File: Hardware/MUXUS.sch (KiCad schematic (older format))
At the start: 124 parts, among them J1 USB_C_Receptacle_USB2.0, J10 VCP, J2 USB_B, J3 USB_A, J4 USB_B, J5 USB_A, J6 STDC14, J7 USB_B, J8 USB_A, J9 SWD, SW1 USER, SW2 RESET, U1 USBLC6-4SC6, U10 AP2151W, U11 AOZ1212AI, U12 USBLC6-2SC6, U13 USBLC6-2SC6, U14 AP2151W, U2 USB2504A-JT, U3 USBLC6-2SC6, U4 USBLC6-2SC6, U5 AP2151W, U6 TS3USBCA420RSVR, U7 STM32G431K8T6, U8 USBLC6-2SC6, U9 USBLC6-2SC6, Y1 ATS240C

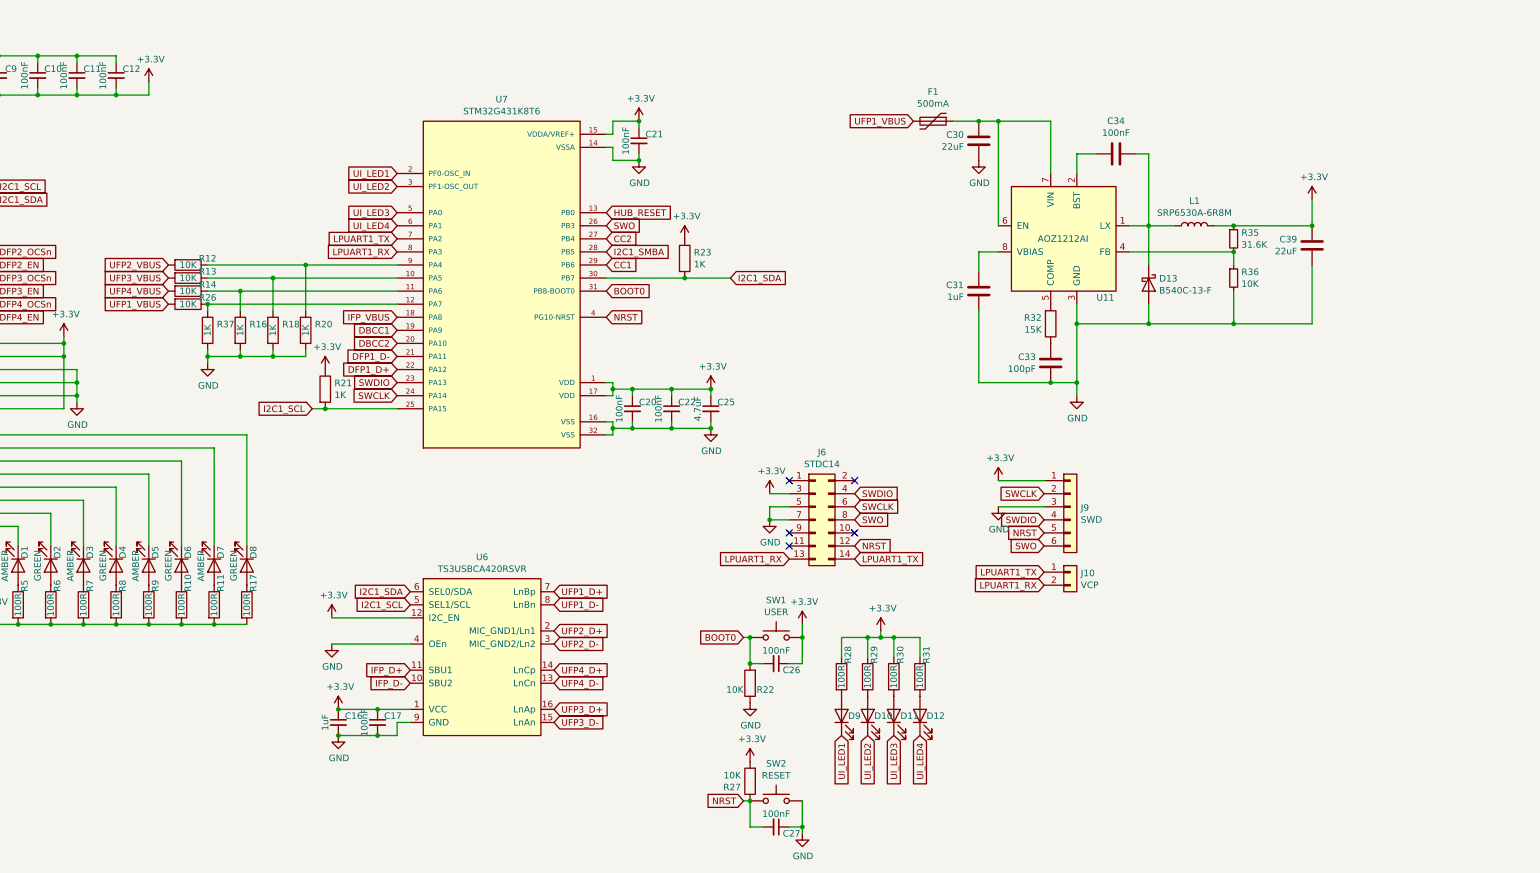
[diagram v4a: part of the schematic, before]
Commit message: Updated STM32G441KBU6
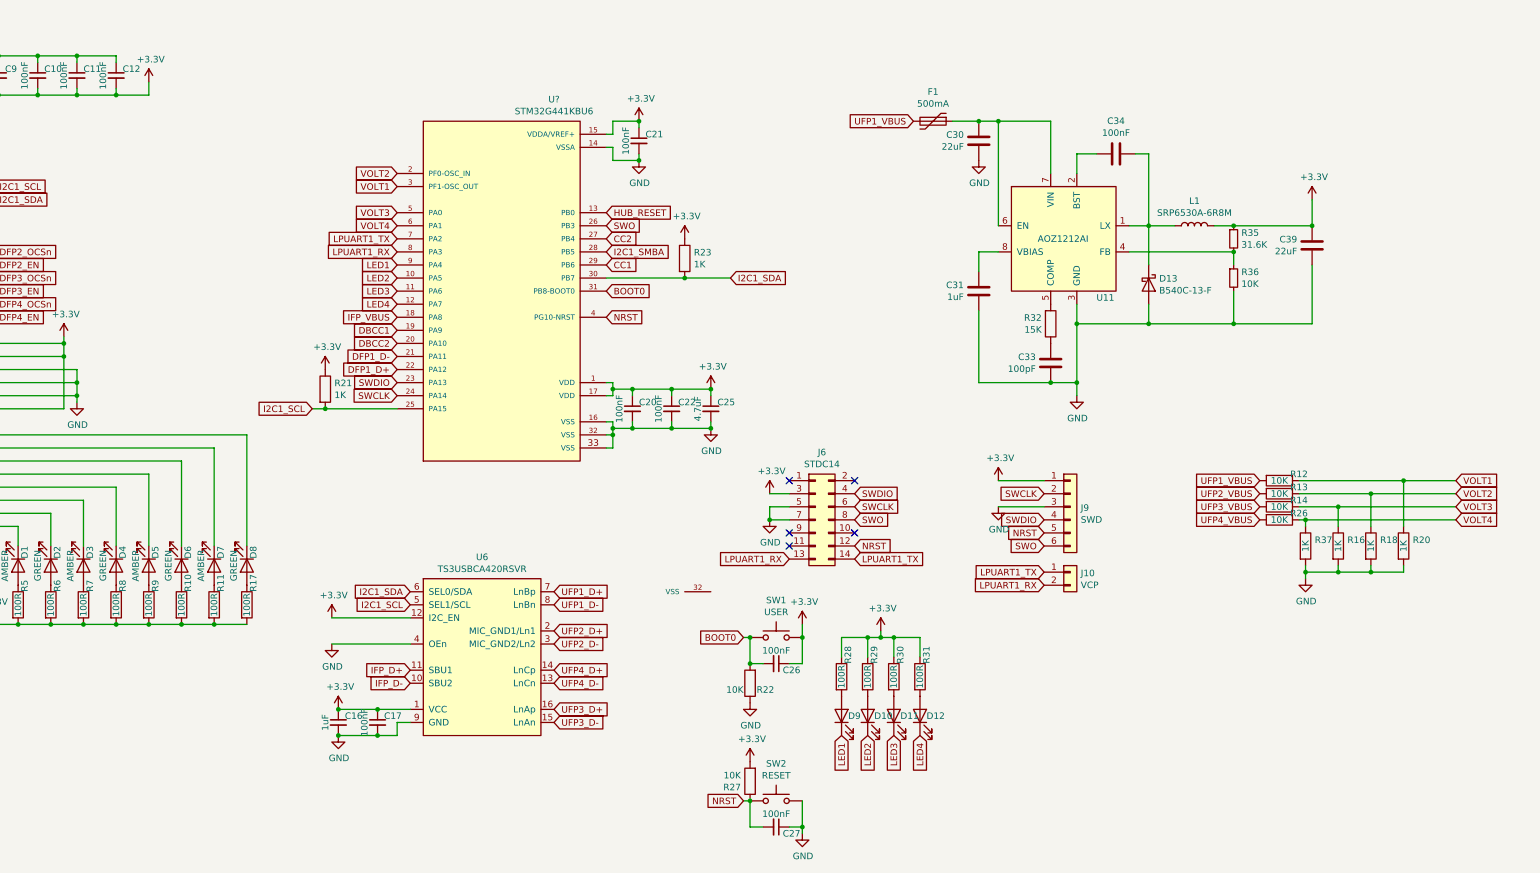
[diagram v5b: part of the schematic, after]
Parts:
- removed U7: STM32G431K8T6, STM32G431K8T6:STM32G431K8T6, symbol STM32G431K8T6:STM32G431K8T6
- added U?: STM32G441KBU6, STM32G441KBU6:STM32G441KBU6, symbol STM32G441KBU6:STM32G441KBU6
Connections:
- net +3V3: now also U?.1 (VDD), U?.15 (VDDA/VREF+), U?.17 (VDD)
- net BOOT0: now also U?.31 (PB8-BOOT0)
- net CC1: now also U?.19 (PA9), U?.29 (PB6)
- net CC2: now also U?.20 (PA10), U?.27 (PB4)
- net DFP1_D+: now also U?.22 (PA12)
- net DFP1_D-: now also U?.21 (PA11)
- net GND: now also U?.14 (VSSA), U?.16 (VSS), U?.32 (VSS), U?.33 (VSS)
- net HUB_RESET: now also U?.13 (PB0)
- net I2C1_SCL: now also U?.25 (PA15)
- net I2C1_SDA: now also U?.30 (PB7)
- net I2C1_SMBA: now also U?.28 (PB5)
- net IFP_VBUS: now also U?.18 (PA8)
- net LPUART1_RX: now also U?.8 (PA3)
- net LPUART1_TX: now also U?.7 (PA2)
- net NRST: now also U?.4 (PG10-NRST)
- net SWCLK: now also U?.24 (PA14)
- net SWDIO: now also U?.23 (PA13)
- net SWO: now also U?.26 (PB3)
- net UFP2_VBUS: now also R13.2; no longer R12.2
- net UFP3_VBUS: now also R14.2; no longer R13.2
- net UFP4_VBUS: now also R26.2; no longer R14.2
- net VBUS: now also R12.2; no longer R26.2
- net VOLT2: now reaches R13.1, R18.1
- net VOLT2: now also U?.2 (PF0-OSC_IN)
- net VOLT3: now reaches R14.1, R16.1
- net VOLT3: now also U?.5 (PA0)
- net VOLT4: now reaches R26.1, R37.1
- net VOLT4: now also U?.6 (PA1)
- net VOLT1: now reaches R12.1, R20.1
- net VOLT1: now also U?.3 (PF1-OSC_OUT)
- net UI_LED1 renamed LED1
- net LED1: now also U?.9 (PA4)
- net UI_LED2 renamed LED2
- net LED2: now also U?.10 (PA5)
- net UI_LED3 renamed LED3
- net LED3: now also U?.11 (PA6)
- net UI_LED4 renamed LED4
- net LED4: now also U?.12 (PA7)
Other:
- moved on the sheet: R12, R13, R14, R16, R18, R20, R26, R37
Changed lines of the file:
@@
 $EndDescr
 $Comp
-L STM32G431K8T6:STM32G431K8T6 U7
-U 1 1 61457F4C
-P 8100 6800
-F 0 "U7" H 8100 8267 50  0000 C CNN
-F 1 "STM32G431K8T6" H 8100 8176 50  0000 C CNN
-F 2 "STM32G431K8T6:STM32G431K8T6" H 8100 6800 50  0001 L BNN
-F 3 "https://www.st.com/en/microcontrollers-microprocessors/stm32g431k8.html#documentation" H 8100 6800 50  0001 L BNN
-F 4 "ST" H 8100 6800 50  0001 L BNN "MANUFACTURER"
-F 5 "2" H 8100 6800 50  0001 L BNN "PARTREV"
-F 6 "1.6mm" H 8100 6800 50  0001 L BNN "MAXIMUN_PACKAGE_HEIGHT"
-F 7 "IPC-7351B" H 8100 6800 50  0001 L BNN "STANDARD"
-	1    8100 6800
-	1    0    0    -1
-$EndComp
-$Comp
 L Device:C_Small C20
 U 1 1 614734E1
@@
 Text GLabel 8900 6200 2    50   Input ~ 0
 HUB_RESET
-Text GLabel 7300 6300 0    50   Input ~ 0
-UI_LED4
-Text GLabel 7300 6200 0    50   Input ~ 0
-UI_LED3
-Text GLabel 7300 6000 0    50   Input ~ 0
-UI_LED2
-Text GLabel 7300 5900 0    50   Input ~ 0
-UI_LED1
+Text GLabel 7300 6900 0    50   Input ~ 0
+LED4
+Text GLabel 7300 6800 0    50   Input ~ 0
+LED3
+Text GLabel 7300 6700 0    50   Input ~ 0
+LED2
+Text GLabel 7300 6600 0    50   Input ~ 0
+LED1
 Text GLabel 4200 6100 2    50   Input ~ 0
 I2C1_SDA
@@
 	4850 7650 4850 7600
 Text GLabel 11300 10200 3    50   Input ~ 0
-UI_LED4
+LED4
 $Comp
 L Device:LED D12
@@
 $EndComp
 Text GLabel 11100 10200 3    50   Input ~ 0
-UI_LED3
+LED3
 $Comp
 L Device:LED D11
@@
 $EndComp
 Text GLabel 10900 10200 3    50   Input ~ 0
-UI_LED2
+LED2
 $Comp
 L Device:LED D10
@@
 $EndComp
 Text GLabel 10700 10200 3    50   Input ~ 0
-UI_LED1
+LED1
 $Comp
 L Device:LED D9
@@
 L Device:R R14
 U 1 1 6241BDE6
-P 5700 6800
-F 0 "R14" V 5650 6950 50  0000 C CNN
-F 1 "10K" V 5700 6800 50  0000 C CNN
-F 2 "Resistor_SMD:R_1206_3216Metric" V 5630 6800 50  0001 C CNN
-F 3 "~" H 5700 6800 50  0001 C CNN
-	1    5700 6800
+P 14050 8450
+F 0 "R14" V 14000 8600 50  0000 C CNN
+F 1 "10K" V 14050 8450 50  0000 C CNN
+F 2 "Resistor_SMD:R_1206_3216Metric" V 13980 8450 50  0001 C CNN
+F 3 "~" H 14050 8450 50  0001 C CNN
+	1    14050 8450
 	0    1    1    0
 $EndComp
@@
 L Device:R R13
 U 1 1 6241B806
-P 5700 6700
-F 0 "R13" V 5650 6850 50  0000 C CNN
-F 1 "10K" V 5700 6700 50  0000 C CNN
-F 2 "Resistor_SMD:R_1206_3216Metric" V 5630 6700 50  0001 C CNN
-F 3 "~" H 5700 6700 50  0001 C CNN
-	1    5700 6700
+P 14050 8350
+F 0 "R13" V 14000 8500 50  0000 C CNN
+F 1 "10K" V 14050 8350 50  0000 C CNN
+F 2 "Resistor_SMD:R_1206_3216Metric" V 13980 8350 50  0001 C CNN
+F 3 "~" H 14050 8350 50  0001 C CNN
+	1    14050 8350
 	0    1    1    0
 $EndComp
@@
 L Device:R R12
 U 1 1 62418C95
-P 5700 6600
-F 0 "R12" V 5650 6750 50  0000 C CNN
-F 1 "10K" V 5700 6600 50  0000 C CNN
-F 2 "Resistor_SMD:R_1206_3216Metric" V 5630 6600 50  0001 C CNN
-F 3 "~" H 5700 6600 50  0001 C CNN
-	1    5700 6600
+P 14050 8250
+F 0 "R12" V 14000 8400 50  0000 C CNN
+F 1 "10K" V 14050 8250 50  0000 C CNN
+F 2 "Resistor_SMD:R_1206_3216Metric" V 13980 8250 50  0001 C CNN
+F 3 "~" H 14050 8250 50  0001 C CNN
+	1    14050 8250
 	0    1    1    0
 $EndComp
-Text GLabel 5550 6800 0    50   Input ~ 0
+Text GLabel 13900 8550 0    50   Input ~ 0
 UFP4_VBUS
-Text GLabel 5550 6700 0    50   Input ~ 0
+Text GLabel 13900 8450 0    50   Input ~ 0
 UFP3_VBUS
-Text GLabel 5550 6600 0    50   Input ~ 0
+Text GLabel 13900 8350 0    50   Input ~ 0
 UFP2_VBUS
 $Comp
 L Device:R R20
 U 1 1 62488B54
-P 6600 7100
-F 0 "R20" H 6670 7146 50  0000 L CNN
-F 1 "1K" V 6600 7100 50  0000 C CNN
-F 2 "Resistor_SMD:R_1206_3216Metric" V 6530 7100 50  0001 C CNN
-F 3 "~" H 6600 7100 50  0001 C CNN
-	1    6600 7100
+P 15000 8750
+F 0 "R20" H 15070 8796 50  0000 L CNN
+F 1 "1K" V 15000 8750 50  0000 C CNN
+F 2 "Resistor_SMD:R_1206_3216Metric" V 14930 8750 50  0001 C CNN
+F 3 "~" H 15000 8750 50  0001 C CNN
+	1    15000 8750
 	1    0    0    -1
 $EndComp
@@
 L Device:R R18
 U 1 1 624DD996
-P 6350 7100
-F 0 "R18" H 6420 7146 50  0000 L CNN
-F 1 "1K" V 6350 7100 50  0000 C CNN
-F 2 "Resistor_SMD:R_1206_3216Metric" V 6280 7100 50  0001 C CNN
-F 3 "~" H 6350 7100 50  0001 C CNN
-	1    6350 7100
+P 14750 8750
+F 0 "R18" H 14820 8796 50  0000 L CNN
+F 1 "1K" V 14750 8750 50  0000 C CNN
+F 2 "Resistor_SMD:R_1206_3216Metric" V 14680 8750 50  0001 C CNN
+F 3 "~" H 14750 8750 50  0001 C CNN
+	1    14750 8750
 	1    0    0    -1
 $EndComp
 $Comp
-L Device:R R16
-U 1 1 624DE01E
-P 6100 7100
-F 0 "R16" H 6170 7146 50  0000 L CNN
-F 1 "1K" V 6100 7100 50  0000 C CNN
-F 2 "Resistor_SMD:R_1206_3216Metric" V 6030 7100 50  0001 C CNN
-F 3 "~" H 6100 7100 50  0001 C CNN
-	1    6100 7100
-	1    0    0    -1
-$EndComp
-Wire Wire Line
-	5850 6800 6100 6800
-$Comp
 L power:GND #PWR015
 U 1 1 6260B042
-P 5850 7350
-F 0 "#PWR015" H 5850 7100 50  0001 C CNN
-F 1 "GND" H 5855 7177 50  0000 C CNN
-F 2 "" H 5850 7350 50  0001 C CNN
-F 3 "" H 5850 7350 50  0001 C CNN
-	1    5850 7350
+P 14250 9000
+F 0 "#PWR015" H 14250 8750 50  0001 C CNN
+F 1 "GND" H 14255 8827 50  0000 C CNN
+F 2 "" H 14250 9000 50  0001 C CNN
+F 3 "" H 14250 9000 50  0001 C CNN
+	1    14250 9000
 	1    0    0    -1
 $EndComp
 Wire Wire Line
-	6350 7300 6100 7300
+	14750 8950 14500 8950
 Wire Wire Line
-	6100 7300 6100 7250
+	14500 8950 14500 8900
 Wire Wire Line
-	6350 7300 6350 7250
-Connection ~ 6350 7300
+	14750 8950 14750 8900
+Connection ~ 14750 8950
 Wire Wire Line
-	6350 7300 6600 7300
+	14750 8950 15000 8950
 Wire Wire Line
-	6600 7300 6600 7250
+	15000 8950 15000 8900
 $Comp
 L power:VBUS #PWR06
@@
 Text GLabel 12250 9050 0    50   Input ~ 0
 LPUART1_RX
-Wire Wire Line
-	5850 6600 6600 6600
-Wire Wire Line
-	5850 6700 6350 6700
 $Comp
 L Device:R R26
 U 1 1 615C410A
-P 5700 6900
-F 0 "R26" V 5650 7050 50  0000 C CNN
-F 1 "10K" V 5700 6900 50  0000 C CNN
-F 2 "Resistor_SMD:R_1206_3216Metric" V 5630 6900 50  0001 C CNN
-F 3 "~" H 5700 6900 50  0001 C CNN
-	1    5700 6900
+P 14050 8550
+F 0 "R26" V 14000 8700 50  0000 C CNN
+F 1 "10K" V 14050 8550 50  0000 C CNN
+F 2 "Resistor_SMD:R_1206_3216Metric" V 13980 8550 50  0001 C CNN
+F 3 "~" H 14050 8550 50  0001 C CNN
+	1    14050 8550
 	0    1    1    0
 $EndComp
-Wire Wire Line
-	7300 6900 5850 6900
 $Comp
 L Device:R R37
 U 1 1 6167BF5A
-P 5850 7100
-F 0 "R37" H 5920 7146 50  0000 L CNN
-F 1 "1K" V 5850 7100 50  0000 C CNN
-F 2 "Resistor_SMD:R_1206_3216Metric" V 5780 7100 50  0001 C CNN
-F 3 "~" H 5850 7100 50  0001 C CNN
-	1    5850 7100
+P 14250 8750
+F 0 "R37" H 14320 8796 50  0000 L CNN
+F 1 "1K" V 14250 8750 50  0000 C CNN
+F 2 "Resistor_SMD:R_1206_3216Metric" V 14180 8750 50  0001 C CNN
+F 3 "~" H 14250 8750 50  0001 C CNN
+	1    14250 8750
 	1    0    0    -1
 $EndComp
-Connection ~ 6100 7300
+Connection ~ 14500 8950
 Wire Wire Line
-	5850 7300 5850 7250
+	14250 8950 14250 8900
 Wire Wire Line
-	5850 7300 6100 7300
+	14250 8950 14500 8950
 Wire Wire Line
-	5850 7350 5850 7300
-Connection ~ 5850 7300
+	14250 9000 14250 8950
+Connection ~ 14250 8950
 Wire Wire Line
-	5850 6950 5850 6900
-Connection ~ 5850 6900
+	14250 8600 14250 8550
 Wire Wire Line
-	6100 6950 6100 6800
-Connection ~ 6100 6800
+	14500 8600 14500 8450
 Wire Wire Line
-	6100 6800 7300 6800
+	14750 8600 14750 8350
 Wire Wire Line
-	6350 6950 6350 6700
-Connection ~ 6350 6700
+	15000 8600 15000 8250
+Text GLabel 13900 8250 0    50   Input ~ 0
+UFP1_VBUS
 Wire Wire Line
-	6350 6700 7300 6700
+	14200 8550 14250 8550
+Connection ~ 14250 8550
+Text GLabel 15400 8250 2    50   Input ~ 0
+VOLT1
+Text GLabel 15400 8350 2    50   Input ~ 0
+VOLT2
+Text GLabel 15400 8450 2    50   Input ~ 0
+VOLT3
+Text GLabel 15400 8550 2    50   Input ~ 0
+VOLT4
+Text GLabel 7300 6000 0    50   Input ~ 0
+VOLT1
+Text GLabel 7300 5900 0    50   Input ~ 0
+VOLT2
+Text GLabel 7300 6200 0    50   Input ~ 0
+VOLT3
+Text GLabel 7300 6300 0    50   Input ~ 0
+VOLT4
+Wire Wire Line
+	14250 8550 15400 8550
+$Comp
+L Device:R R16
+U 1 1 624DE01E
+P 14500 8750
+F 0 "R16" H 14570 8796 50  0000 L CNN
+F 1 "1K" V 14500 8750 50  0000 C CNN
+F 2 "Resistor_SMD:R_1206_3216Metric" V 14430 8750 50  0001 C CNN
+F 3 "~" H 14500 8750 50  0001 C CNN
+	1    14500 8750
+	1    0    0    -1
+$EndComp
+Connection ~ 14500 8450
 Wire Wire Line
-	6600 6950 6600 6600
-Connection ~ 6600 6600
+	14500 8450 15400 8450
 Wire Wire Line
-	6600 6600 7300 6600
-Text GLabel 5550 6900 0    50   Input ~ 0
-UFP1_VBUS
+	14200 8450 14500 8450
+Connection ~ 14750 8350
+Wire Wire Line
+	14750 8350 15400 8350
+Wire Wire Line
+	14200 8350 14750 8350
+Connection ~ 15000 8250
+Wire Wire Line
+	15000 8250 15400 8250
+Wire Wire Line
+	14200 8250 15000 8250
+$Comp
+L STM32G441KBU6:STM32G441KBU6 U?
+U 1 1 6191BD86
+P 8100 6800
+F 0 "U?" H 8500 8267 50  0000 C CNN
+F 1 "STM32G441KBU6" H 8500 8176 50  0000 C CNN
+F 2 "STM32G441KBU6:STM32G441KBU6" H 8100 6800 50  0001 L BNN
+F 3 "" H 8100 6800 50  0001 L BNN
+F 4 "ST" H 8100 6800 50  0001 L BNN "MANUFACTURER"
+F 5 "2" H 8100 6800 50  0001 L BNN "PARTREV"
+F 6 "1.6mm" H 8100 6800 50  0001 L BNN "MAXIMUN_PACKAGE_HEIGHT"
+F 7 "IPC-7351B" H 8100 6800 50  0001 L BNN "STANDARD"
+	1    8100 6800
+	1    0    0    -1
+$EndComp
+Wire Wire Line
+	8900 8000 8950 8000
+Wire Wire Line
+	8950 8000 8950 7900
+Connection ~ 8950 7900
 $EndSCHEMATC
